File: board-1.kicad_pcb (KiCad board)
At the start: 2 copper layers, 52.7 x 38.1 mm, 23 parts, among them P1 CONN_01X03, P2 USB_B_fixed, P3 CONN_01X07, P4 CONN_01X05, P5 CONN_01X02, U1 MCP1700, U2 PIC32MX2XX, Y1 24MHz

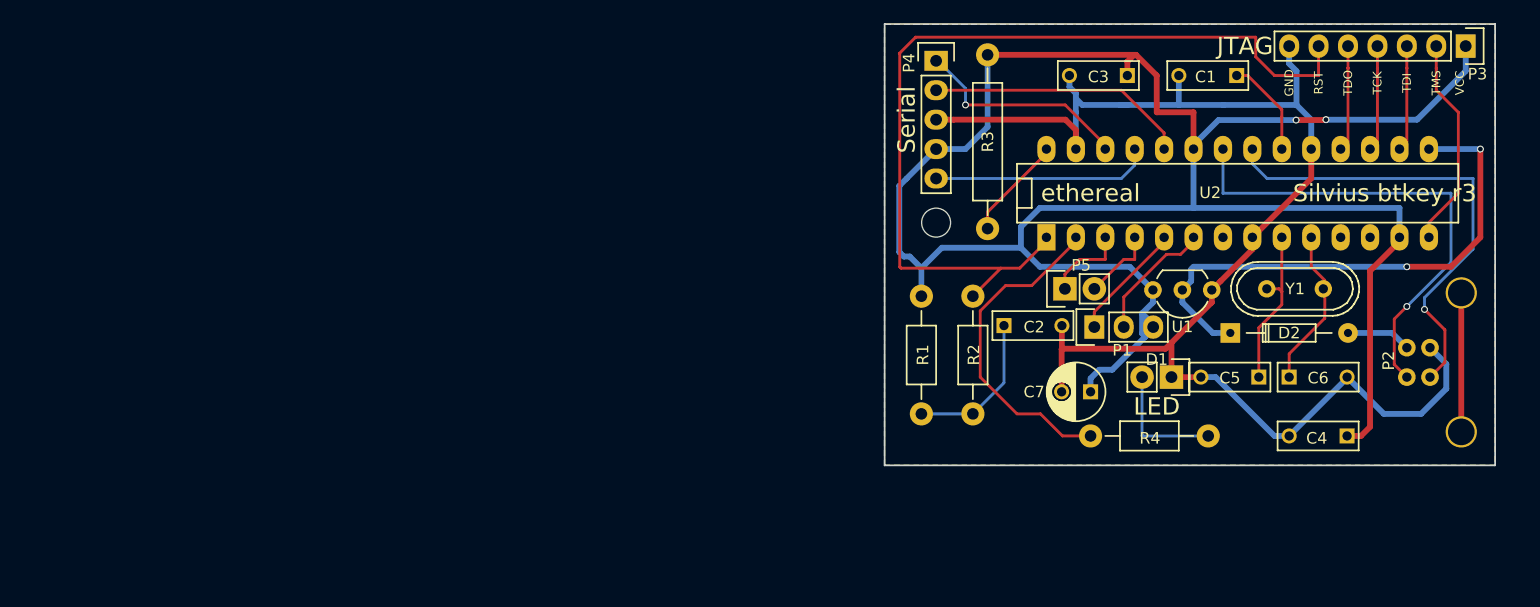
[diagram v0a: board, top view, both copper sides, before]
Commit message: Changes for r4.
Major change: a board that fits in a 5cmx5cm square.
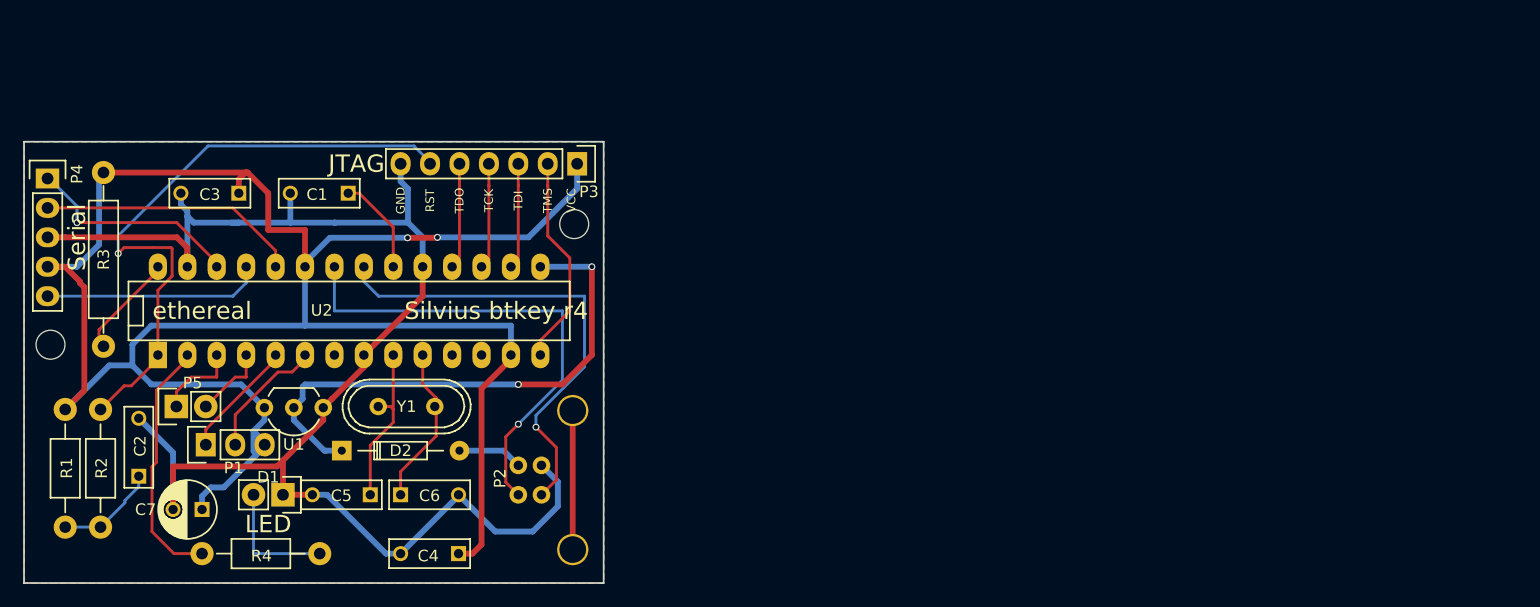
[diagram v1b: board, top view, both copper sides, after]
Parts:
- added REF**: MountingHole_2-5mm, Mounting_Holes:MountingHole_2-5mm, F.Cu at (98.3, 57.9)
- moved C3 77.4 mm to (69.3, 55.2)
- moved C4 77.4 mm to (88.3, 86.4)
- moved C5 77.4 mm to (80.7, 81.3)
- moved C6 77.4 mm to (83.3, 81.3)
- moved D1 77.4 mm to (73.2, 81.3)
- moved R4 77.4 mm to (71.2, 86.4)
- moved C1 77.4 mm to (78.8, 55.2)
- moved C7 77.4 mm to (66.2, 82.5)
- moved D2 77.4 mm to (78.2, 77.5)
- moved P2 77.4 mm to (93.5, 81.3)
- moved P4 77.4 mm to (52.8, 54.0)
- moved P5 77.4 mm to (64.0, 73.7)
- moved U1 77.4 mm to (76.6, 73.8)
- moved Y1 77.4 mm to (83.8, 73.7)
- moved P1 77.4 mm to (66.5, 77.0)
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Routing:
- net /RST: track 77.7 -> 54.3 mm, vias 0 -> 1
- net GND: track 128.1 -> 135.2 mm
- net /StatusLED: track 28.4 -> 21.6 mm
- net Net-(C2-Pad1): track 13.2 -> 8.81 mm
- net +3V3: track 181.1 -> 179.1 mm
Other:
- board size 52.7 x 38.1 mm -> 50 x 38.1 mm
- board text added: "Shrink target"
- board text added: "Silvius btkey r4"
- board text added: "Silvius project by dwk@voxhub.io Hardware r1-4 by ethereal@ethv.net"
- board text removed: "Silvius btkey r3"
- board text removed: "Silvius project by dwk@voxhub.io Hardware r1-3 by ethereal@ethv.net"
